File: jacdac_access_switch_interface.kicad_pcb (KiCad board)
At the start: 2 copper layers, 35 x 35 mm, 42 parts, among them J1 Conn_Jacdac_CardEdge, J2 Conn_HackConnect, J3 jack_3.5_pj313d, J4 jack_3.5_pj313d, SW1 SW_PTS810, U1 NCP114ASN330T1G, U2 STM32G030F6P6, U3 TLP240A, U4 TLP240A

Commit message: Routing in progress
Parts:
- moved C4 1.84 mm to (157.9, 80.1), turned to 180 degrees
- moved R2 0.91 mm to (167.2, 95.5), turned to 0 degrees
- moved D3 0.63 mm to (151.1, 76.1), turned to 180 degrees
- moved R3 0.46 mm to (163.4, 70.7)
- moved D5 0.38 mm to (163.4, 99.2)
- moved R6 0.38 mm to (162.3, 97.2)
- moved R7 0.38 mm to (163.3, 97.2)
- moved R8 0.38 mm to (164.4, 97.2)
- moved D2 0.36 mm to (153.5, 90.3)
- moved R13 0.28 mm to (153.5, 87.5)
- moved R1 0.22 mm to (153.7, 75.5)
- moved R4 0.21 mm to (167.1, 76.3)
- moved R5 0.20 mm to (169.0, 82.4)
- moved C3 0.14 mm to (153.7, 77.5)
- moved FB1 0.14 mm to (153.7, 79.5)
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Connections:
- U2 pad 11: /SLEEVE2_P -> /RELAY2
- U2 pad 12: /RING2_P -> /SLEEVE2_P
- U2 pad 13: /TIP2_P -> /RING2_P
- U2 pad 14: /RELAY2 -> /TIP2_P
- U4 pad 3: /SLEEVE1 -> /TIP1
- U4 pad 4: /TIP1 -> /SLEEVE1
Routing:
- net +3V3: track 32.0 -> 82.1 mm
- net /RELAY2: track 0.00 -> 31.9 mm, vias 0 -> 4
- net /nRESET: track 3.76 -> 25.9 mm, vias 0 -> 2
- net /RELAY1: track 0.00 -> 13.4 mm, vias 0 -> 4
- net /RGB_B: track 0.00 -> 10.6 mm
- net /RGB_G: track 0.00 -> 10.1 mm, vias 0 -> 2
- net /TIP1: track 15.8 -> 25.9 mm
- net /SLEEVE1: track 7.30 -> 17.0 mm
- net /RGB_R: track 0.00 -> 9.62 mm, vias 0 -> 2
- net /RING1_P: track 11.3 -> 19.9 mm, vias 0 -> 2
- net /SWDCLK: track 2.73 -> 10.9 mm
- net /TIP1_P: track 8.58 -> 16.7 mm, vias 0 -> 2
- net /SWDIO: track 3.61 -> 11.5 mm
- net /SLEEVE1_P: track 9.57 -> 17.1 mm, vias 0 -> 2
- net /JD_DATA: track 9.62 -> 3.37 mm
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- added copper zone on F.Cu, net GND

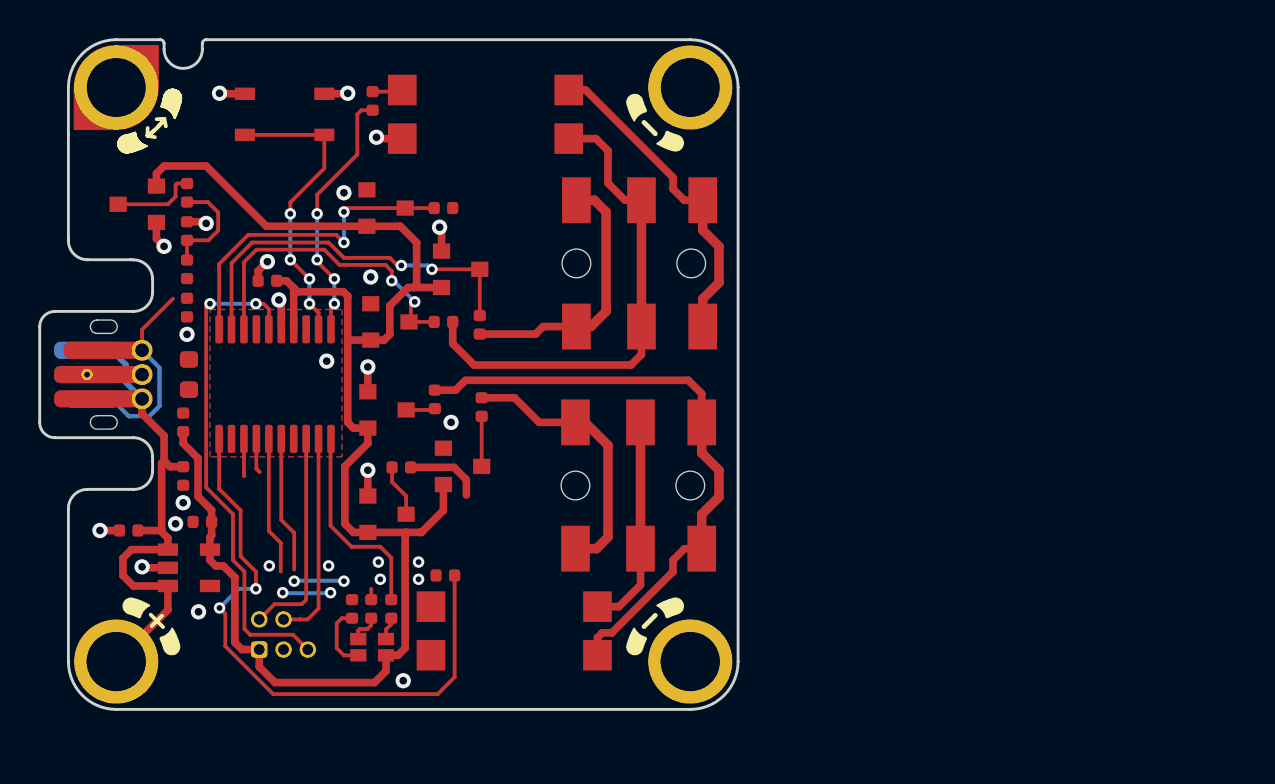
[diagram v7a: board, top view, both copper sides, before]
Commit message: Last commit before re-assigning pins on MCU and spinning MCU
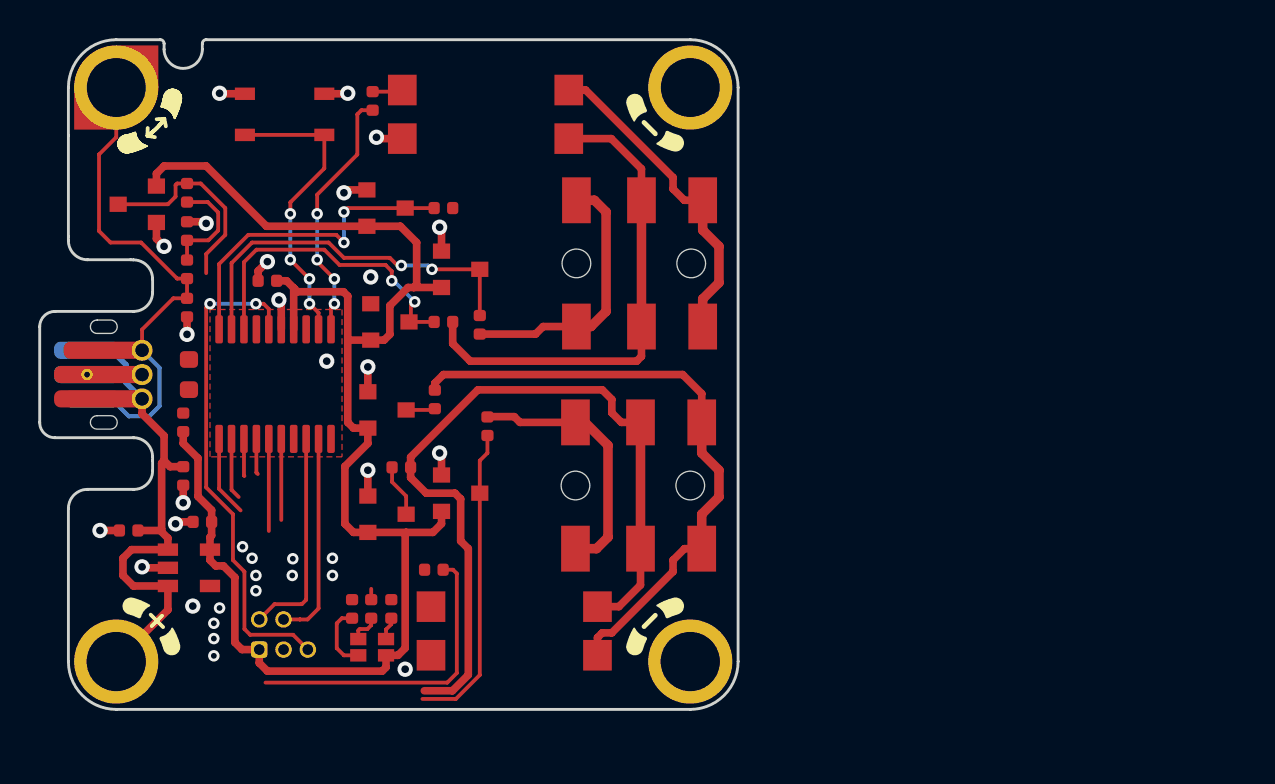
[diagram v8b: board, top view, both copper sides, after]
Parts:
- J3: value jack_3.5_pj313d -> pj313d
- moved D9 1.40 mm to (168.0, 91.2)
- moved R11 1.04 mm to (169.4, 87.7)
- moved R2 0.67 mm to (166.6, 95.2)
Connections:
- D3 pad 3: Net-(D3-common) -> /JD_DATA_MCU
- R1 pad 1: Net-(D3-common) -> /JD_DATA_MCU
- U2 pad 17: /JD_DATA_MCU -> unconnected-(U2-PA12[PA10])
- U2 pad 20: /RGB_B -> /JD_DATA_MCU
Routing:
- net /TIP2: track 15.2 -> 42.0 mm
- net /JD_DATA: track 3.37 -> 18.6 mm
- net /RING2_P: track 4.58 -> 18.1 mm, vias 4 -> 2
- net /RELAY2: track 31.9 -> 20.4 mm, vias 4 -> 2
- net /JD_DATA_MCU: track 0.00 -> 10.7 mm
- net /RGB_B: track 10.6 -> 0.00 mm
- net /RGB_G: track 10.1 -> 4.84 mm
- net GND: track 15.5 -> 20.8 mm
- net /RGB_R: track 9.62 -> 4.81 mm
- net Net-(D3-common): track 4.40 -> 0.00 mm
- net /SLEEVE2_P: track 1.53 -> 4.72 mm, vias 0 -> 2
- net +3V3: track 82.1 -> 80.3 mm
- net /RING2: track 14.4 -> 13.7 mm
- net /SLEEVE2: track 31.9 -> 32.4 mm
- net /TIP2_P: track 4.56 -> 4.62 mm, vias 0 -> 2
